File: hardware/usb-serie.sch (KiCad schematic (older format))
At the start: 13 parts

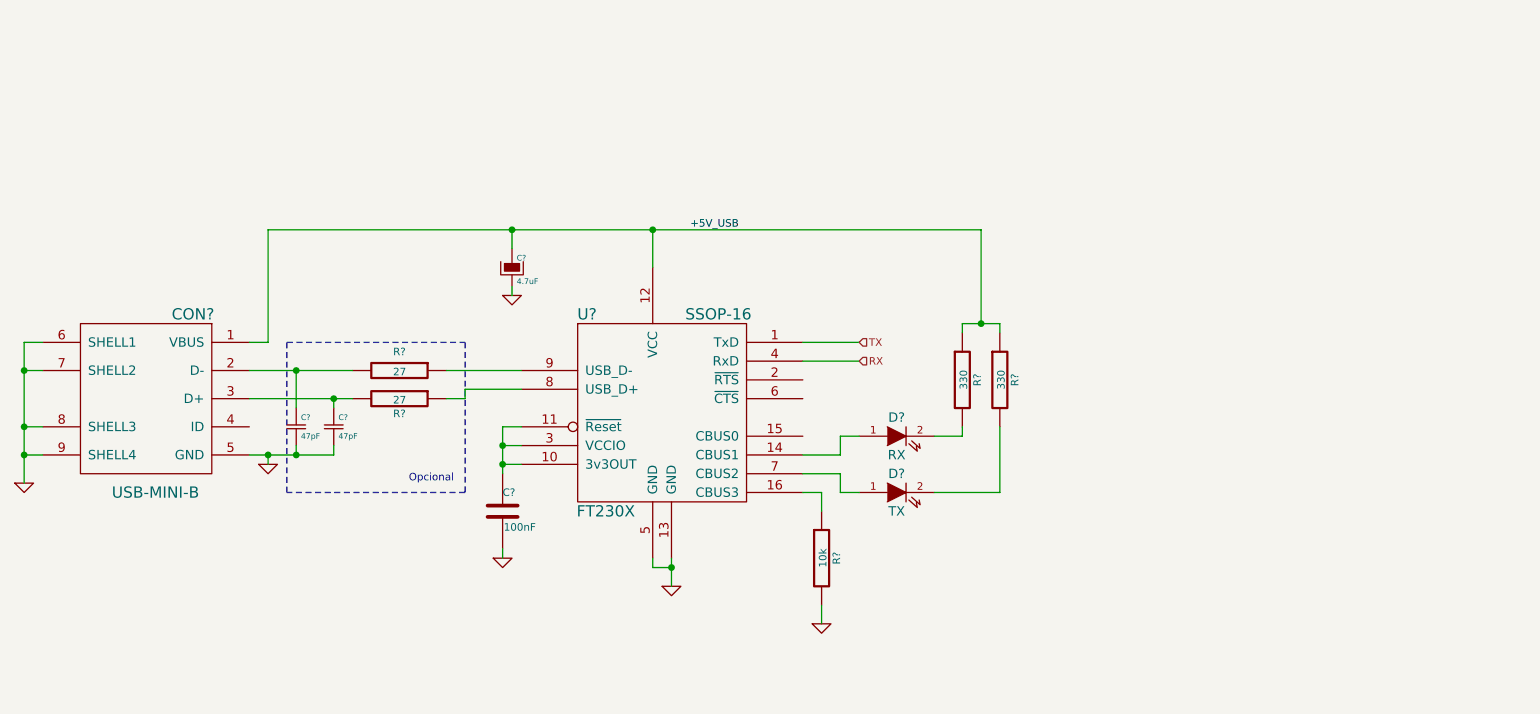
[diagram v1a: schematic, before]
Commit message: Se agrego alimentacion por USB-Serie, falta fuente
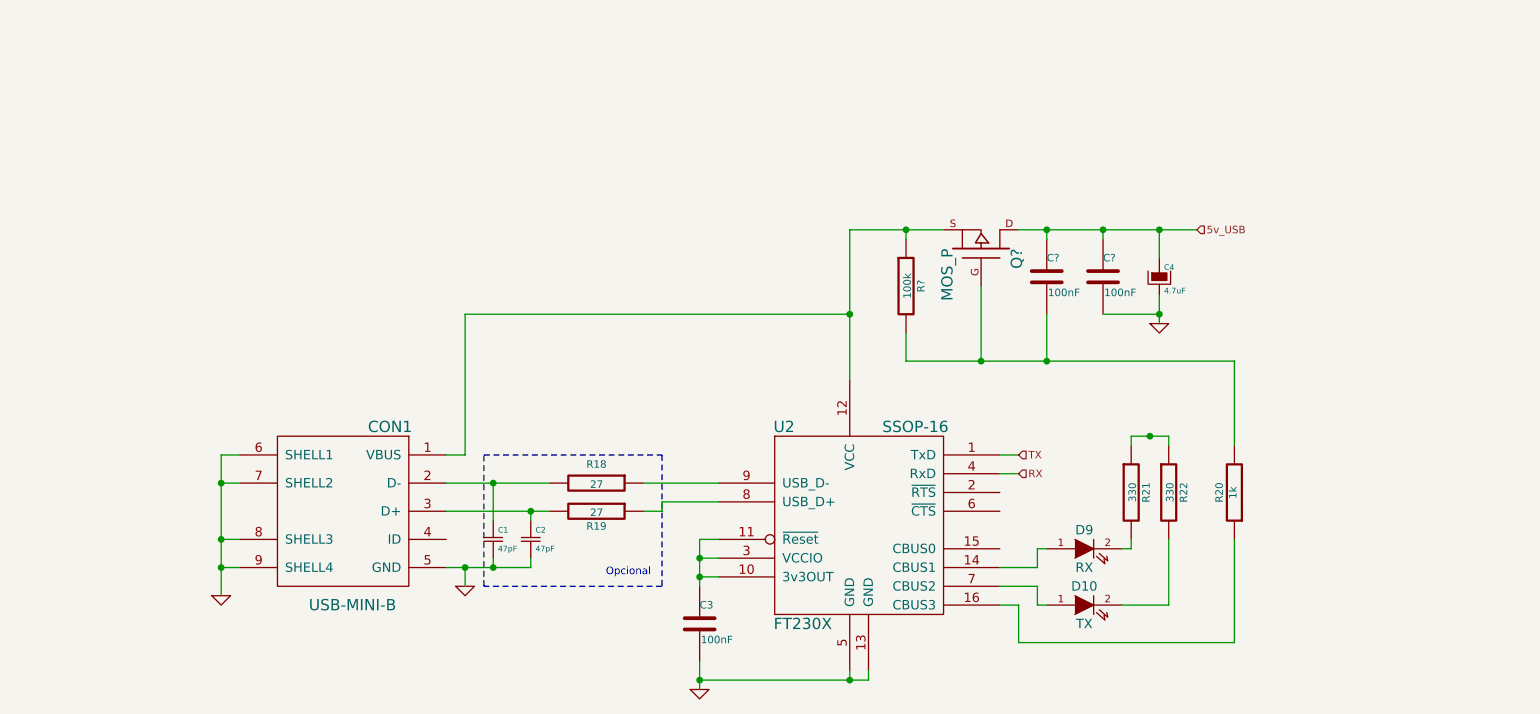
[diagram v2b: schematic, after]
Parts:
- added C? (x2): 100nF, symbol C
- added Q?: MOS_P, symbol MOS_P
- added R?: 100k, symbol R
- R20: renamed from R?; value 10k -> 1k
- gave numbers to parts that had none: 12
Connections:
- net GND: now also C?.2; no longer R20.2
- removed net +5V_USB: C4.1, CON1.1 (VBUS), R21.1, R22.1, U2.12 (VCC)
- new net: CON1.1 (VBUS), Q?.S, R?.1, U2.12 (VCC)
- new net: C?.2, Q?.G, R20.2, R?.2
- new net: R21.1, R22.1
- new net 5v_USB: C4.1, C?.1, C?.1, Q?.D
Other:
- moved on the sheet: C1, C2, C3, C4, CON1, D10, D9, R18, R19, R20, R21, R22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

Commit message: Se agrego SD, se colocaron pins en varios modulos, se corrigio orden del VGA
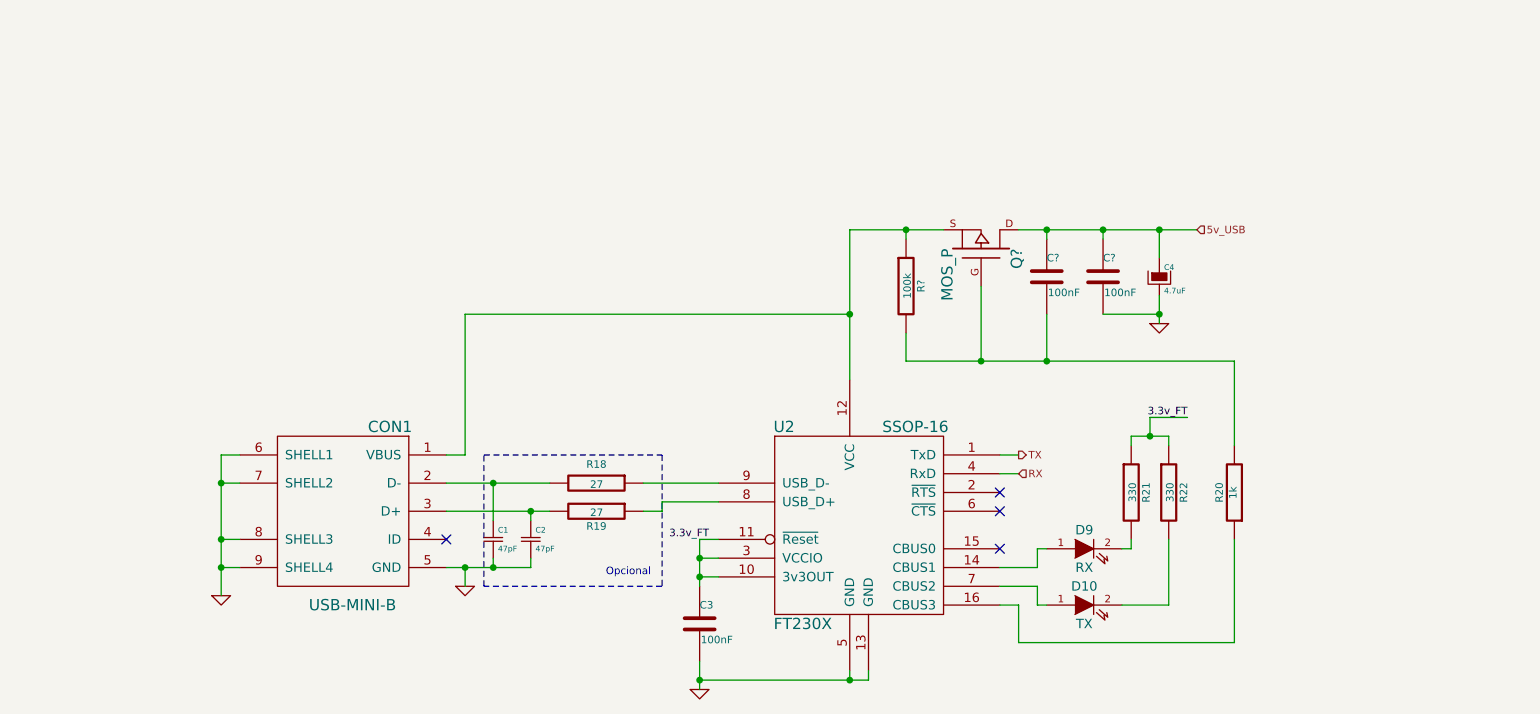
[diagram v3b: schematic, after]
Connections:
- net 3.3v_FT: now reaches C3.1, U2.10 (3v3OUT), U2.11 (~Reset), U2.3 (VCCIO)
- net 3.3v_FT: now also R21.1, R22.1
- no-connect marks 0 -> 4
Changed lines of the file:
@@
 LIBS:serial
 LIBS:oscillator-cmos-out-4
+LIBS:con-yamaichi-cf-2
 LIBS:STM32F4-UCC-cache
 EELAYER 24 0
@@
 $Descr A4 11693 8268
 encoding utf-8
-Sheet 2 5
+Sheet 2 6
 Title ""
 Date ""
@@
 	5550 4150 5450 4150
 Wire Wire Line
-	5450 4150 5450 4250
-Wire Wire Line
-	5450 4250 5450 4350
-Wire Wire Line
-	5450 4350 5450 4400
+	5450 4150 5450 4400
 Wire Wire Line
 	5450 4350 5550 4350
@@
 $EndComp
 Wire Wire Line
-	5450 4800 5450 4900
-Wire Wire Line
-	5450 4900 5450 4950
+	5450 4800 5450 4950
 Connection ~ 5450 4350
 Wire Wire Line
 	6250 4850 6250 4900
 Wire Wire Line
-	5450 4900 6250 4900
-Wire Wire Line
-	6250 4900 6350 4900
+	5450 4900 6350 4900
 $Comp
 L R R20
@@
 	7150 4500 7150 4700
 Wire Wire Line
-	4100 4000 4550 4000
-Wire Wire Line
-	4550 4000 4650 4000
+	4100 4000 4650 4000
 Wire Wire Line
 	4200 3700 4100 3700
@@
 	4200 4400 4200 4300
 Wire Wire Line
-	4100 4300 4200 4300
-Wire Wire Line
-	4200 4300 4350 4300
-Wire Wire Line
-	4350 4300 4550 4300
+	4100 4300 4550 4300
 $Comp
 L GND #PWR26
@@
 $EndComp
 Wire Wire Line
-	2900 3700 2900 3850
-Wire Wire Line
-	2900 3850 2900 4150
-Wire Wire Line
-	2900 4150 2900 4300
-Wire Wire Line
-	2900 4300 2900 4450
+	2900 3700 2900 4450
 Wire Wire Line
 	2900 3700 3000 3700
@@
 	7750 3650 7750 3600
 Wire Wire Line
-	7750 3600 7850 3600
-Wire Wire Line
-	7850 3600 7950 3600
+	7750 3600 7950 3600
 Wire Wire Line
 	7950 3600 7950 3650
@@
 $EndComp
 Wire Wire Line
-	4100 3850 4350 3850
-Wire Wire Line
-	4350 3850 4650 3850
+	4100 3850 4650 3850
 Wire Wire Line
 	5150 3850 5550 3850
@@
 Text Notes 4950 4350 0    40   ~ 0
 Opcional
-Text HLabel 7150 3700 2    40   Input ~ 0
+Text HLabel 7150 3700 2    40   Output ~ 0
 TX
 Text HLabel 7150 3800 2    40   Input ~ 0
@@
 	7300 2550 7300 2500
 Wire Wire Line
-	7150 2500 7300 2500
-Wire Wire Line
-	7300 2500 7600 2500
-Wire Wire Line
-	7600 2500 7900 2500
-Wire Wire Line
-	7900 2500 8100 2500
+	7150 2500 8100 2500
 $Comp
 L C C?
@@
 Connection ~ 7900 2950
 Wire Wire Line
-	7900 2850 7900 2950
-Wire Wire Line
-	7900 2950 7900 3000
+	7900 2850 7900 3000
 Connection ~ 5450 4900
 Connection ~ 6250 4900
@@
 	6950 2800 6950 3200
 Wire Wire Line
-	6550 3200 6950 3200
-Wire Wire Line
-	6950 3200 7300 3200
-Wire Wire Line
-	7300 3200 8300 3200
+	6550 3200 8300 3200
 Wire Wire Line
 	8300 4700 8300 4150
@@
 	8300 3200 8300 3650
 Wire Wire Line
-	6250 2500 6550 2500
-Wire Wire Line
-	6550 2500 6750 2500
-Wire Wire Line
-	6250 2500 6250 2950
-Wire Wire Line
-	6250 2950 6250 3300
+	6250 2500 6750 2500
+Wire Wire Line
+	6250 2500 6250 3300
 Wire Wire Line
 	4200 2950 6250 2950
@@
 5v_USB
 Connection ~ 7900 2500
+Text Label 5500 4150 2    40   ~ 0
+3.3v_FT
+Text Label 8050 3500 2    40   ~ 0
+3.3v_FT
+Wire Wire Line
+	7850 3600 7850 3500
+Wire Wire Line
+	7850 3500 8050 3500
+NoConn ~ 7050 3900
+NoConn ~ 7050 4000
+NoConn ~ 7050 4200
+NoConn ~ 4100 4150
 $EndSCHEMATC

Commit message: Terminado el esquematico, iniciado el PCB
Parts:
- added C18: 10nf, Capacitors_SMD:c_1206, symbol Csmall
- added C19: 100nF, Capacitors_SMD:c_1206, symbol Csmall
- added C20: 4.7uF, Capacitors_ThroughHole:Capacitor5x11RM2.5, symbol CPsmall
- added L1: MI0805K601R-10, Resistors_SMD:Resistor_SMD0805_ReflowWave, symbol INDUCTOR_SMALL
- added R62, R63: 10k, Resistors_SMD:Resistor_SMD1206_ReflowWave, symbol R
- C1, C2, C3: footprint (none) -> Capacitors_SMD:c_1206
- C15, C16: renamed from C?; footprint (none) -> Capacitors_SMD:c_1206
- C4: footprint (none) -> Capacitors_ThroughHole:Capacitor5x11RM2.5
- D10, D9: footprint (none) -> LEDs:LED-0805
- Q1: renamed from Q?; value MOS_P -> IRLML6402; footprint (none) -> SMD_Packages:SOT-23
- R18, R19, R20, R21, R22: footprint (none) -> Resistors_SMD:Resistor_SMD1206_ReflowWave
- R49: renamed from R?; footprint (none) -> Resistors_SMD:Resistor_SMD1206_ReflowWave
- U2: footprint SSOP-16 -> Housings_SSOP:SSOP-16
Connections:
- net 3.3v_FT: now also R62.1, R63.1
- net GND: now also C18.2, C19.2, C20.2
- net RX: now also R63.2
- net TX: now also R62.2
- net at Q1.S, R49.1, U2.12 (VCC): now also C19.1, C20.1, L1.2; no longer CON1.1 (VBUS)
- net at U2.14 (CBUS1): now also D9.2 (K); no longer D9.1 (A)
- net at U2.7 (CBUS2): now also D10.2 (K); no longer D10.1 (A)
- net at R21.2: now also D9.1 (A); no longer D9.2 (K)
- net at R22.2: now also D10.1 (A); no longer D10.2 (K)
- new net: C18.1, CON1.1 (VBUS), L1.1
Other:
- moved on the sheet: C15, C16, C4, Q1, R49

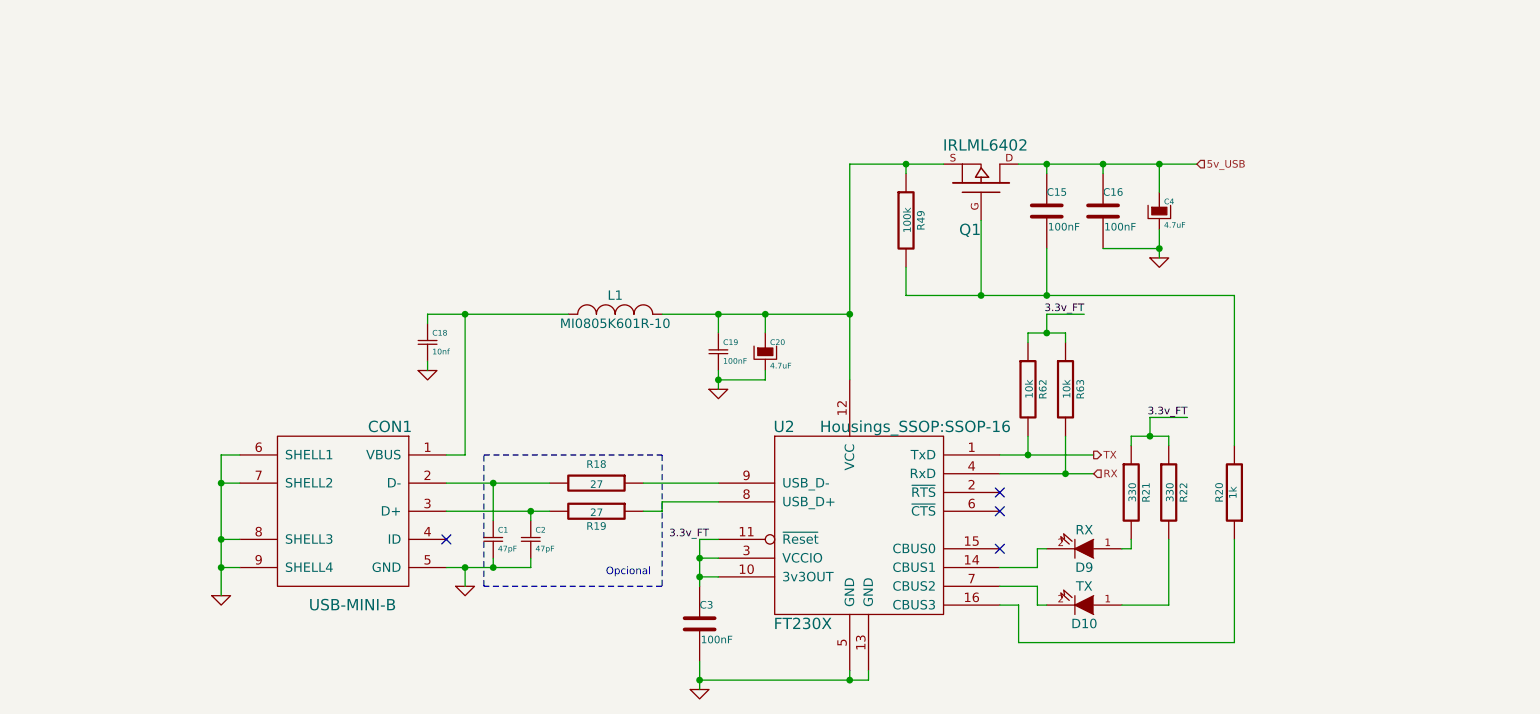
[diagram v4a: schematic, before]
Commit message: Terminado el Routeo de la Placa
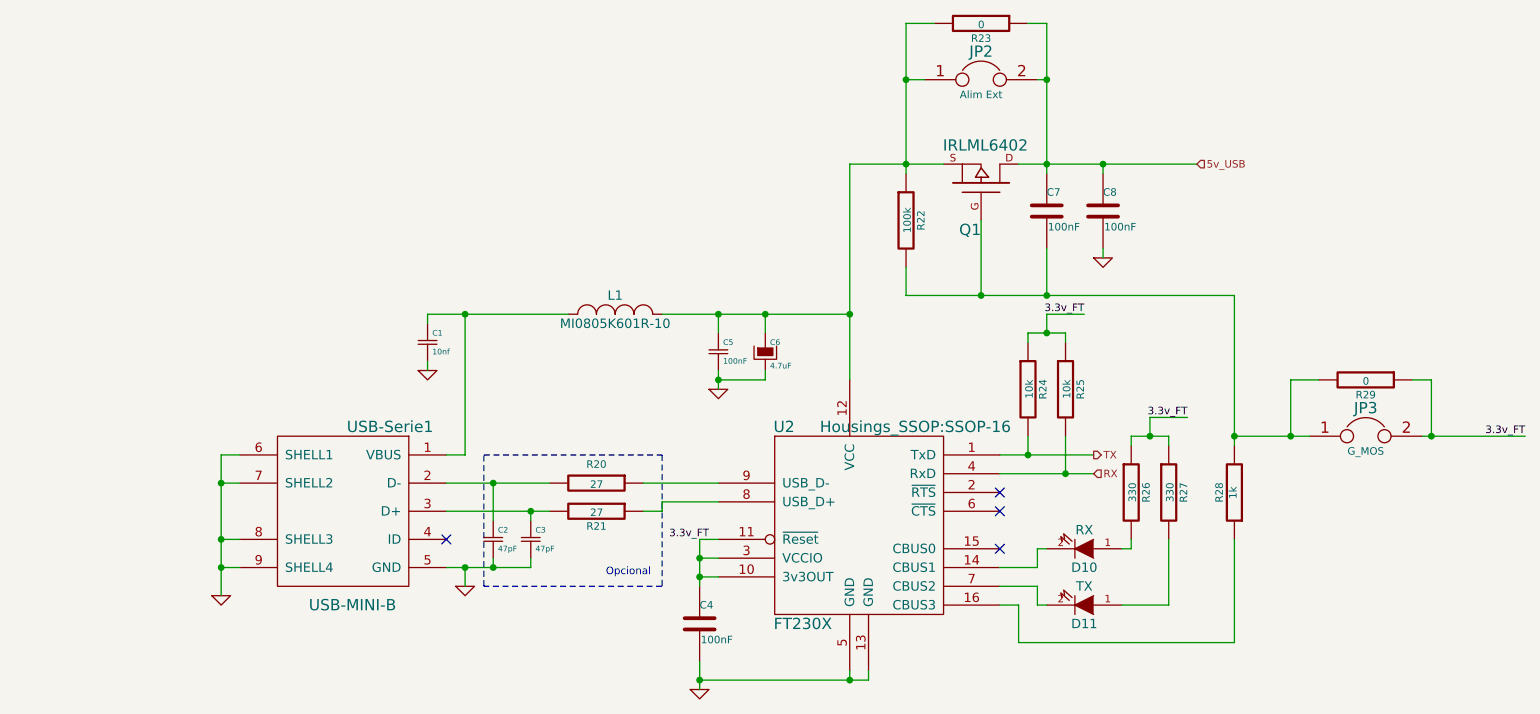
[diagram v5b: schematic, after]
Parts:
- removed C4: 4.7uF, Capacitors_ThroughHole:Capacitor5x11RM2.5, symbol CPsmall
- added JP2: Alim Ext, Pin_Headers:Pin_Header_Straight_1x02, symbol JUMPER
- added JP3: G_MOS, Pin_Headers:Pin_Header_Straight_1x02, symbol JUMPER
- added R23, R29: 0, Resistors_SMD:R_0805, symbol R
- C1: renamed from C18; footprint Capacitors_SMD:c_1206 -> Capacitors_SMD:c_0805
- C2: renamed from C1; footprint Capacitors_SMD:c_1206 -> Capacitors_SMD:c_0805
- C3: renamed from C2; footprint Capacitors_SMD:c_1206 -> Capacitors_SMD:c_0805
- C4: renamed from C3; footprint Capacitors_SMD:c_1206 -> Capacitors_SMD:c_0805
- C5: renamed from C19; footprint Capacitors_SMD:c_1206 -> Capacitors_SMD:c_0805
- C7: renamed from C15; footprint Capacitors_SMD:c_1206 -> Capacitors_SMD:c_0805
- C8: renamed from C16; footprint Capacitors_SMD:c_1206 -> Capacitors_SMD:c_0805
- L1: footprint Resistors_SMD:Resistor_SMD0805_ReflowWave -> Resistors_SMD:R_0805
- Q1: footprint SMD_Packages:SOT-23 -> SMD_Packages:SOT-23-GDS
- R20: renamed from R18; footprint Resistors_SMD:Resistor_SMD1206_ReflowWave -> Resistors_SMD:R_0805
- R21: renamed from R19; footprint Resistors_SMD:Resistor_SMD1206_ReflowWave -> Resistors_SMD:R_0805
- R22: renamed from R49; footprint Resistors_SMD:Resistor_SMD1206_ReflowWave -> Resistors_SMD:R_0805
- R24: renamed from R62; footprint Resistors_SMD:Resistor_SMD1206_ReflowWave -> Resistors_SMD:R_0805
- R25: renamed from R63; footprint Resistors_SMD:Resistor_SMD1206_ReflowWave -> Resistors_SMD:R_0805
- R26: renamed from R21; footprint Resistors_SMD:Resistor_SMD1206_ReflowWave -> Resistors_SMD:R_0805
- R27: renamed from R22; footprint Resistors_SMD:Resistor_SMD1206_ReflowWave -> Resistors_SMD:R_0805
- R28: renamed from R20; footprint Resistors_SMD:Resistor_SMD1206_ReflowWave -> Resistors_SMD:R_0805
- USB-Serie1: renamed from CON1; footprint (none) -> w_Connectors:Micro_USB_type_B
- renumbered C20 to C6, D9 to D10, D10 to D11
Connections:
- net 3.3v_FT: now also JP3.2, R29.1
- net 5v_USB: now also JP2.2, R23.1
- net at C5.1, C6.1, L1.2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: now also JP2.1, R23.2
- net at C7.2, Q1.G, R22.2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: now also JP3.1, R29.2

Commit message: Placa terminada, serigrafia verificada, logos agregados
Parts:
- C1, C2, C3, C4, C5, C7, C8: footprint Capacitors_SMD:c_0805 -> w_Connectors:c_0805
- D10, D11: footprint LEDs:LED-0805 -> w_Connectors:Led_0805
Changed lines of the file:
@@
 F 0 "C4" H 5450 4700 40  0000 L CNN
 F 1 "100nF" H 5456 4515 40  0000 L CNN
-F 2 "Capacitors_SMD:c_0805" H 5488 4450 30  0001 C CNN
+F 2 "w_Connectors:c_0805" H 5488 4450 30  0001 C CNN
 F 3 "" H 5450 4600 60  0000 C CNN
 	1    5450 4600
@@
 F 0 "D10" H 7500 4300 50  0000 C CNN
 F 1 "RX" H 7500 4100 50  0000 C CNN
-F 2 "LEDs:LED-0805" H 7500 4200 60  0001 C CNN
+F 2 "w_Connectors:Led_0805" H 7500 4200 60  0001 C CNN
 F 3 "" H 7500 4200 60  0000 C CNN
 	1    7500 4200
@@
 F 0 "D11" H 7500 4600 50  0000 C CNN
 F 1 "TX" H 7500 4400 50  0000 C CNN
-F 2 "LEDs:LED-0805" H 7500 4500 60  0001 C CNN
+F 2 "w_Connectors:Led_0805" H 7500 4500 60  0001 C CNN
 F 3 "" H 7500 4500 60  0000 C CNN
 	1    7500 4500
@@
 F 0 "C2" H 4375 4200 30  0000 L CNN
 F 1 "47pF" H 4375 4100 30  0000 L CNN
-F 2 "Capacitors_SMD:c_0805" H 4350 4150 60  0001 C CNN
+F 2 "w_Connectors:c_0805" H 4350 4150 60  0001 C CNN
 F 3 "" H 4350 4150 60  0000 C CNN
 	1    4350 4150
@@
 F 0 "C3" H 4575 4200 30  0000 L CNN
 F 1 "47pF" H 4575 4100 30  0000 L CNN
-F 2 "Capacitors_SMD:c_0805" H 4550 4150 60  0001 C CNN
+F 2 "w_Connectors:c_0805" H 4550 4150 60  0001 C CNN
 F 3 "" H 4550 4150 60  0000 C CNN
 	1    4550 4150
@@
 F 0 "C7" H 7300 2500 40  0000 L CNN
 F 1 "100nF" H 7306 2315 40  0000 L CNN
-F 2 "Capacitors_SMD:c_0805" H 7338 2250 30  0001 C CNN
+F 2 "w_Connectors:c_0805" H 7338 2250 30  0001 C CNN
 F 3 "" H 7300 2400 60  0000 C CNN
 	1    7300 2400
@@
 F 0 "C8" H 7600 2500 40  0000 L CNN
 F 1 "100nF" H 7606 2315 40  0000 L CNN
-F 2 "Capacitors_SMD:c_0805" H 7638 2250 30  0001 C CNN
+F 2 "w_Connectors:c_0805" H 7638 2250 30  0001 C CNN
 F 3 "" H 7600 2400 60  0000 C CNN
 	1    7600 2400
@@
 F 0 "C1" H 4025 3150 30  0000 L CNN
 F 1 "10nf" H 4025 3050 30  0000 L CNN
-F 2 "Capacitors_SMD:c_0805" H 4000 3100 60  0001 C CNN
+F 2 "w_Connectors:c_0805" H 4000 3100 60  0001 C CNN
 F 3 "" H 4000 3100 60  0000 C CNN
 	1    4000 3100
@@
 F 0 "C5" H 5575 3200 30  0000 L CNN
 F 1 "100nF" H 5575 3100 30  0000 L CNN
-F 2 "Capacitors_SMD:c_0805" H 5550 3150 60  0001 C CNN
+F 2 "w_Connectors:c_0805" H 5550 3150 60  0001 C CNN
 F 3 "" H 5550 3150 60  0000 C CNN
 	1    5550 3150
